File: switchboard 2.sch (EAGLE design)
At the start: 185 parts, among them IC1 MT8816AP, IC10 Z8F2480SO, IC11 LMV321M5, IC12 74HC595D, IC14 74LVC1G125DBV, IC15 74LVC1G125DBV, IC16 LM2940-9, IC17 PC817S OPTO, IC2 NE5532D, IC3 TC7660-SOIC, IC4 TC7660-SOIC, IC5 FT232RL, IC6 78L05F, IC7 LD117AS33TR, IC8 SPI_MEMORY-SOIC, IC9 NE5532D, Q3 BSS84, X1 MINI-USB-SCHIELD-32005-301

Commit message: Series resistors added to all audio effects inputs and outputs. Overvoltage protection added to audio and MIDI outputs. ESD protection added to MIDI inputs and outputs. USB_DETECT signal added to UART pinheader.
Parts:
- added D15, D16, D17, D18, D7, D8: LL4148, diode:DIODE-MINIMELF
- added GAP10, GAP7, GAP8, GAP9: SPARK_GAP, PATSKO:SPARK_GAP
- added R10, R11, R12, R13, R56, R57, R58, R59, R72, R73, R74, R75, R76, R77, R78, R79, R80, R9: 100, rcl:R-US_R0603
- P_UART: device pinhead:PINHD-1X3 -> pinhead:PINHD-1X4
- Q3: value BSS84 -> FDN352AP
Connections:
- new net N$65: C49.2, R59.2
- new net N$66: C50.2, R72.2
- new net N$67: C51.2, R73.2
- new net N$68: C52.2, R74.2
- new net N$69: JP27.3, R10.1
- new net N$70: JP27.9, R13.1
- new net N$71: JP27.7, R12.1
- new net N$72: JP27.5, R11.1
- new net N$73: JP28.3, R58.1
- new net N$74: JP28.9, R73.1
- new net N$75: JP28.5, R59.1
- new net N$76: JP28.7, R72.1
- net +5V_AN: now also D15.C, D7.C
- net 3V3_MIDI: now also D17.C
- net GND: now also D16.A, D18.A, D8.A, GAP7.2, GAP8.1, P_UART.4; no longer P_UART.1
- net GND1: now also GAP10.2, GAP9.1
- net MIDI_IN1: now also GAP9.2
- net MIDI_IN2: now also GAP10.1
- net MIDI_OUT1: now also GAP7.1
- net MIDI_OUT2: now also GAP8.2
- net N$12: now also R9.1; no longer C35.2
- net N$14: now also D7.A, D8.C
- net N$15: now also C35.2, R9.2; no longer C36.2, JP27.3
- net N$16: now also C36.2, R10.2; no longer C37.2, JP27.5
- net N$17: now also C37.2, R11.2; no longer C38.2, JP27.7
- net N$18: now also C38.2, R12.2; no longer C39.2, JP27.9
- net N$19: now also R56.1; no longer C40.2
- net N$2: now also D17.A, D18.C
- net N$21: now also R75.1; no longer C41.2
- net N$32: now also R76.1; no longer C42.2
- net N$49: now also C39.2, R13.2; no longer C48.2, JP28.3
- net N$50: now also C40.2, R56.2; no longer C49.2, JP28.5
- net N$51: now also C47.2, R57.2; no longer C50.2, JP28.7
- net N$52: now also R77.1; no longer C43.2
- net N$53: now also R78.1; no longer C44.2
- net N$56: now also D15.A, D16.C
- net N$59: now also R79.1; no longer C45.2
- net N$62: now also R80.1; no longer C46.2
- net N$63: now also C48.2, R58.2; no longer C51.2, JP28.9
- net N$64: now also R74.1; no longer C52.2
- net N$9: now also R57.1; no longer C47.2
- net UART_RX: now also P_UART.3; no longer P_UART.2
- net UART_TX: now also P_UART.2; no longer P_UART.3
- net USB_DETECT: now also P_UART.1
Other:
- moved on the sheet: C35, C36, C37, C38, C39, C40, C47, C48, C49, C50, C51, C52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

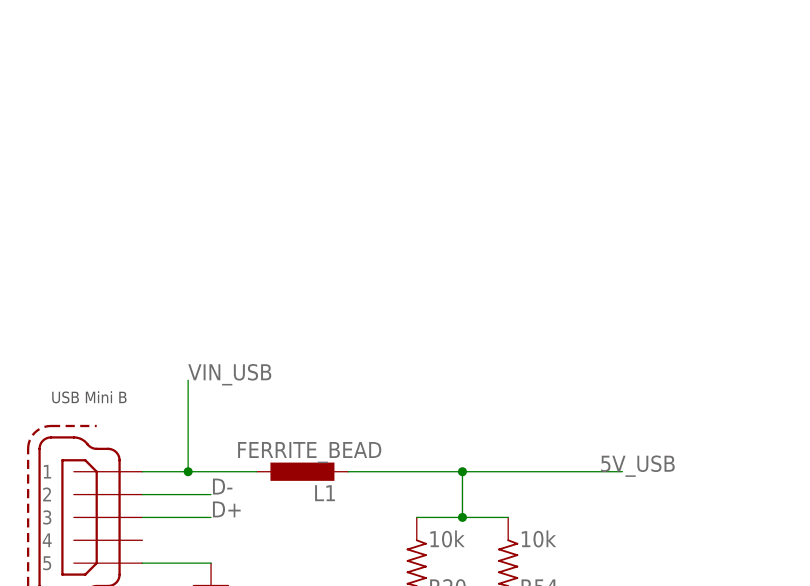
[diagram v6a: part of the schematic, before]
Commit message: ESD protection with TPD2E001 added to USB inputs.
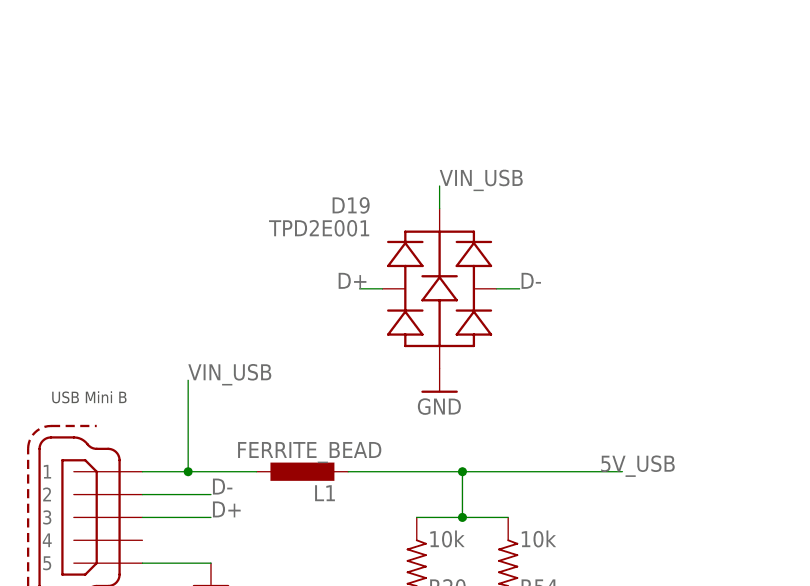
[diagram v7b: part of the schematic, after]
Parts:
- added D19: (no value), PATSKO:TPD2E001
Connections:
- net D+: now also D19.IO1
- net D-: now also D19.IO2
- net GND: now also D19.GND
- net VIN_USB: now also D19.VCC
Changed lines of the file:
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@@
 <part name="SUPPLY9" library="supply2" library_urn="urn:adsk.eagle:library:372" deviceset="GND1" device=""/>
 <part name="P_UART" library="pinhead" deviceset="PINHD-1X4" device=""/>
+<part name="D19" library="PATSKO" deviceset="TPD2E001" device=""/>
+<part name="GND97" library="supply1" deviceset="GND" device=""/>
 </parts>
 <sheets>
@@
 <instance part="SUPPLY9" gate="G$1" x="-434.34" y="246.38" rot="R180"/>
 <instance part="P_UART" gate="A" x="111.76" y="-43.18"/>
+<instance part="D19" gate="G$1" x="-419.1" y="124.46"/>
+<instance part="GND97" gate="1" x="-419.1" y="113.03"/>
 </instances>
 <busses>
@@
 <pinref part="GAP8" gate="G$1" pin="1"/>
 <pinref part="GND89" gate="1" pin="GND"/>
+</segment>
+<segment>
+<pinref part="D19" gate="G$1" pin="GND"/>
+<pinref part="GND97" gate="1" pin="GND"/>
 </segment>
 </net>
@@
 <label x="-444.5" y="43.18" size="1.778" layer="95"/>
 </segment>
+<segment>
+<pinref part="D19" gate="G$1" pin="IO2"/>
+<wire x1="-412.75" y1="124.46" x2="-410.21" y2="124.46" width="0.1524" layer="91"/>
+<label x="-410.21" y="124.46" size="1.778" layer="95"/>
+</segment>
 </net>
 <net name="D+" class="0">
@@
 <pinref part="JP11" gate="A" pin="3"/>
 <label x="-444.5" y="40.64" size="1.778" layer="95"/>
+</segment>
+<segment>
+<pinref part="D19" gate="G$1" pin="IO1"/>
+<wire x1="-425.45" y1="124.46" x2="-427.99" y2="124.46" width="0.1524" layer="91"/>
+<label x="-430.53" y="124.46" size="1.778" layer="95"/>
 </segment>
 </net>
@@
 <label x="-444.5" y="45.72" size="1.778" layer="95"/>
 </segment>
-</net>
+<segment>
+<pinref part="D19" gate="G$1" pin="VCC"/>
+<wire x1="-419.1" y1="133.35" x2="-419.1" y2="135.89" width="0.1524" layer="91"/>
+<label x="-419.1" y="135.89" size="1.778" layer="95"/>
+</segment>
+</net>

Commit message: Layout development. Minor component name and package changes.
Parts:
- C10, C11, C2, C6: device rcl:CPOL-EUE2.5-6 -> PATSKO:CAP_POL
- C30: device rcl:C-EUC0805 -> rcl:C-EUC0603
- renumbered JP1 to JP_POWEREFF1, JP10 to JP_BTNS1, JP11 to JP_USB, JP15 to JP_BTNS2, JP18 to JP_OUTS1, JP2 to JP_POWEREFF2, JP24 to JP_DBG, JP26 to JP_AUDIOEFF3, JP27 to JP_AUDIOEFF1, JP28 to JP_AUDIOEFF2, JP3 to JP_POWEREFF3, P_OUT1 to P_OUT2
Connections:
- new net N$77: C43.2, R77.2
- new net N$78: C41.2, R75.2
- new net N$79: C42.2, R76.2
- new net N$80: C44.2, R78.2
- new net N$81: C45.2, R79.2
- new net N$82: C46.2, R80.2
- net N$14: now also C10.-; no longer C6.-
- net N$27: now also C6.+; no longer C10.+
- net N$54: now also C6.-; no longer C10.-
- net N$8: now also C10.+; no longer C6.+
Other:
- moved on the sheet: C10, C6
